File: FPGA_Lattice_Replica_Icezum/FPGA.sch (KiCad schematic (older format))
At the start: 33 parts, among them U1 iCE40HX1K-TQ144, U2 N25Q032A

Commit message: se finalizo asignación de footprint de acuerdo al modelo original de la icezum alhambra
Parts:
- C12, C13, C14, C15, C16: footprint (none) -> footprints:C_0402
- FID1, FID2, FID3: footprint (none) -> footprints:Fiducial
- LD10: footprint (none) -> footprints:LED_0603
- R1, R2, R3, R4, R46, R5, R6, R7, R8, R9: footprint (none) -> footprints:R_0402
- U1: footprint (none) -> footprints:TQFP-144_IPC-MD
- U2: footprint (none) -> footprints:DFN-8-6x5mm
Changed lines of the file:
@@
 F 0 "U1" H 1950 1587 60  0000 C CNN
 F 1 "iCE40HX1K-TQ144" H 1950 1481 60  0000 C CNN
-F 2 "" H 1600 100 60  0001 C CNN
+F 2 "footprints:TQFP-144_IPC-MD" H 1600 100 60  0001 C CNN
 F 3 "" H 1600 100 60  0000 C CNN
 	1    1250 1300
@@
 F 0 "U1" H 2550 4887 60  0000 C CNN
 F 1 "iCE40HX1K-TQ144" H 2550 4781 60  0000 C CNN
-F 2 "" H 2200 3400 60  0001 C CNN
+F 2 "footprints:TQFP-144_IPC-MD" H 2200 3400 60  0001 C CNN
 F 3 "" H 2200 3400 60  0000 C CNN
 	2    1850 4600
@@
 F 0 "U1" H 6150 1617 60  0000 C CNN
 F 1 "iCE40HX1K-TQ144" H 6150 1511 60  0000 C CNN
-F 2 "" H 5800 150 60  0001 C CNN
+F 2 "footprints:TQFP-144_IPC-MD" H 5800 150 60  0001 C CNN
 F 3 "" H 5800 150 60  0000 C CNN
 	3    5450 1350
@@
 F 0 "U1" H 9400 1617 60  0000 C CNN
 F 1 "iCE40HX1K-TQ144" H 9400 1511 60  0000 C CNN
-F 2 "" H 9050 150 60  0001 C CNN
+F 2 "footprints:TQFP-144_IPC-MD" H 9050 150 60  0001 C CNN
 F 3 "" H 9050 150 60  0000 C CNN
 	4    8700 1350
@@
 F 0 "U1" H 5600 5467 60  0000 C CNN
 F 1 "iCE40HX1K-TQ144" H 5600 5361 60  0000 C CNN
-F 2 "" H 5250 4000 60  0001 C CNN
+F 2 "footprints:TQFP-144_IPC-MD" H 5250 4000 60  0001 C CNN
 F 3 "" H 5250 4000 60  0000 C CNN
 	5    4900 5200
@@
 F 0 "U1" H 9850 4717 60  0000 C CNN
 F 1 "iCE40HX1K-TQ144" H 9850 4611 60  0000 C CNN
-F 2 "" H 9500 3250 60  0001 C CNN
+F 2 "footprints:TQFP-144_IPC-MD" H 9500 3250 60  0001 C CNN
 F 3 "" H 9500 3250 60  0000 C CNN
 	6    9150 4450
@@
 F 0 "R2" V 4750 2700 50  0000 C CNN
 F 1 "10K±5% 0.063W" V 4900 2550 50  0000 C CNN
-F 2 "" V 4730 2550 50  0001 C CNN
+F 2 "footprints:R_0402" V 4730 2550 50  0001 C CNN
 F 3 "~" H 4800 2550 50  0001 C CNN
 	1    4800 2550
@@
 F 0 "R3" V 4650 3000 50  0000 C CNN
 F 1 "10K±5% 0.063W" V 4850 3000 50  0000 C CNN
-F 2 "" V 4680 3000 50  0001 C CNN
+F 2 "footprints:R_0402" V 4680 3000 50  0001 C CNN
 F 3 "~" H 4750 3000 50  0001 C CNN
 	1    4750 3000
@@
 F 0 "R1" V 4693 2200 50  0000 C CNN
 F 1 "10K±5% 0.063W" V 4784 2200 50  0000 C CNN
-F 2 "" V 4830 2200 50  0001 C CNN
+F 2 "footprints:R_0402" V 4830 2200 50  0001 C CNN
 F 3 "~" H 4900 2200 50  0001 C CNN
 	1    4900 2200
@@
 F 0 "U2" H 7350 5400 60  0000 C CNN
 F 1 "N25Q032A" H 7400 4800 60  0000 C CNN
-F 2 "" H 7180 5300 60  0001 C CNN
+F 2 "footprints:DFN-8-6x5mm" H 7180 5300 60  0001 C CNN
 F 3 "" H 7180 5300 60  0000 C CNN
 	1    6650 5200
@@
 F 0 "LD10" H 5143 6745 50  0000 C CNN
 F 1 "Yellow" H 5143 6836 50  0000 C CNN
-F 2 "" H 5150 7000 50  0001 C CNN
+F 2 "footprints:LED_0603" H 5150 7000 50  0001 C CNN
 F 3 "~" H 5150 7000 50  0001 C CNN
 	1    5150 7000
@@
 F 0 "R6" H 7700 4750 50  0000 L CNN
 F 1 "10K±5% 0.063W" V 7600 4250 50  0000 L CNN
-F 2 "" V 7630 4600 50  0001 C CNN
+F 2 "footprints:R_0402" V 7630 4600 50  0001 C CNN
 F 3 "~" H 7700 4600 50  0001 C CNN
 	1    7700 4600
@@
 F 0 "R7" H 7950 4750 50  0000 L CNN
 F 1 "10K±5% 0.063W" V 7850 4250 50  0000 L CNN
-F 2 "" V 7880 4600 50  0001 C CNN
+F 2 "footprints:R_0402" V 7880 4600 50  0001 C CNN
 F 3 "~" H 7950 4600 50  0001 C CNN
 	1    7950 4600
@@
 F 0 "R8" H 8200 4750 50  0000 L CNN
 F 1 "10K±5% 0.063W" V 8100 4250 50  0000 L CNN
-F 2 "" V 8130 4600 50  0001 C CNN
+F 2 "footprints:R_0402" V 8130 4600 50  0001 C CNN
 F 3 "~" H 8200 4600 50  0001 C CNN
 	1    8200 4600
@@
 F 0 "R46" V 5543 7000 50  0000 C CNN
 F 1 "2K2±5% 0.063W" V 5634 7000 50  0000 C CNN
-F 2 "" V 5680 7000 50  0001 C CNN
+F 2 "footprints:R_0402" V 5680 7000 50  0001 C CNN
 F 3 "~" H 5750 7000 50  0001 C CNN
 	1    5750 7000
@@
 F 0 "R5" H 6520 4496 50  0000 L CNN
 F 1 "10K±5% 0.063W" V 6350 4150 50  0000 L CNN
-F 2 "" V 6380 4450 50  0001 C CNN
+F 2 "footprints:R_0402" V 6380 4450 50  0001 C CNN
 F 3 "~" H 6450 4450 50  0001 C CNN
 	1    6450 4450
@@
 F 0 "R4" V 1293 6000 50  0000 C CNN
 F 1 "10K±5% 0.063W" V 1384 6000 50  0000 C CNN
-F 2 "" V 1430 6000 50  0001 C CNN
+F 2 "footprints:R_0402" V 1430 6000 50  0001 C CNN
 F 3 "~" H 1500 6000 50  0001 C CNN
 	1    1500 6000
@@
 F 0 "C12" H 9000 5550 50  0000 L CNN
 F 1 "100 nF" H 9015 5455 50  0000 L CNN
-F 2 "" H 8938 5350 50  0001 C CNN
+F 2 "footprints:C_0402" H 8938 5350 50  0001 C CNN
 F 3 "~" H 8900 5500 50  0001 C CNN
 	1    8900 5500
@@
 F 0 "R9" H 8520 5146 50  0000 L CNN
 F 1 "100K±5% 0.063W" V 8350 4800 50  0000 L CNN
-F 2 "" V 8380 5100 50  0001 C CNN
+F 2 "footprints:R_0402" V 8380 5100 50  0001 C CNN
 F 3 "~" H 8450 5100 50  0001 C CNN
 	1    8450 5100
@@
 F 0 "C16" H 10815 6096 50  0000 L CNN
 F 1 "100 nF" H 10750 5950 50  0000 L CNN
-F 2 "" H 10738 5900 50  0001 C CNN
+F 2 "footprints:C_0402" H 10738 5900 50  0001 C CNN
 F 3 "~" H 10700 6050 50  0001 C CNN
 	1    10700 6050
@@
 F 0 "C15" H 10415 6096 50  0000 L CNN
 F 1 "100 nF" H 10350 5950 50  0000 L CNN
-F 2 "" H 10338 5900 50  0001 C CNN
+F 2 "footprints:C_0402" H 10338 5900 50  0001 C CNN
 F 3 "~" H 10300 6050 50  0001 C CNN
 	1    10300 6050
@@
 F 0 "C14" H 10015 6096 50  0000 L CNN
 F 1 "100 nF" H 9950 5950 50  0000 L CNN
-F 2 "" H 9938 5900 50  0001 C CNN
+F 2 "footprints:C_0402" H 9938 5900 50  0001 C CNN
 F 3 "~" H 9900 6050 50  0001 C CNN
 	1    9900 6050
@@
 F 0 "C13" H 9650 6100 50  0000 L CNN
 F 1 "100 nF" H 9550 5950 50  0000 L CNN
-F 2 "" H 9588 5900 50  0001 C CNN
+F 2 "footprints:C_0402" H 9588 5900 50  0001 C CNN
 F 3 "~" H 9550 6050 50  0001 C CNN
 	1    9550 6050
@@
 F 0 "FID1" H 1678 7303 59  0000 L CNN
 F 1 "FIDUCIAL" H 1678 7198 59  0000 L CNN
-F 2 "" H 1450 7250 157 0001 C CNN
+F 2 "footprints:Fiducial" H 1450 7250 157 0001 C CNN
 F 3 "" H 1450 7250 157 0000 C CNN
 	1    1450 7250
@@
 F 0 "FID2" H 2728 7303 59  0000 L CNN
 F 1 "FIDUCIAL" H 2728 7198 59  0000 L CNN
-F 2 "" H 2500 7250 157 0001 C CNN
+F 2 "footprints:Fiducial" H 2500 7250 157 0001 C CNN
 F 3 "" H 2500 7250 157 0000 C CNN
 	1    2500 7250
@@
 F 0 "FID3" H 3678 7303 59  0000 L CNN
 F 1 "FIDUCIAL" H 3678 7198 59  0000 L CNN
-F 2 "" H 3450 7250 157 0001 C CNN
+F 2 "footprints:Fiducial" H 3450 7250 157 0001 C CNN
 F 3 "" H 3450 7250 157 0000 C CNN
 	1    3450 7250

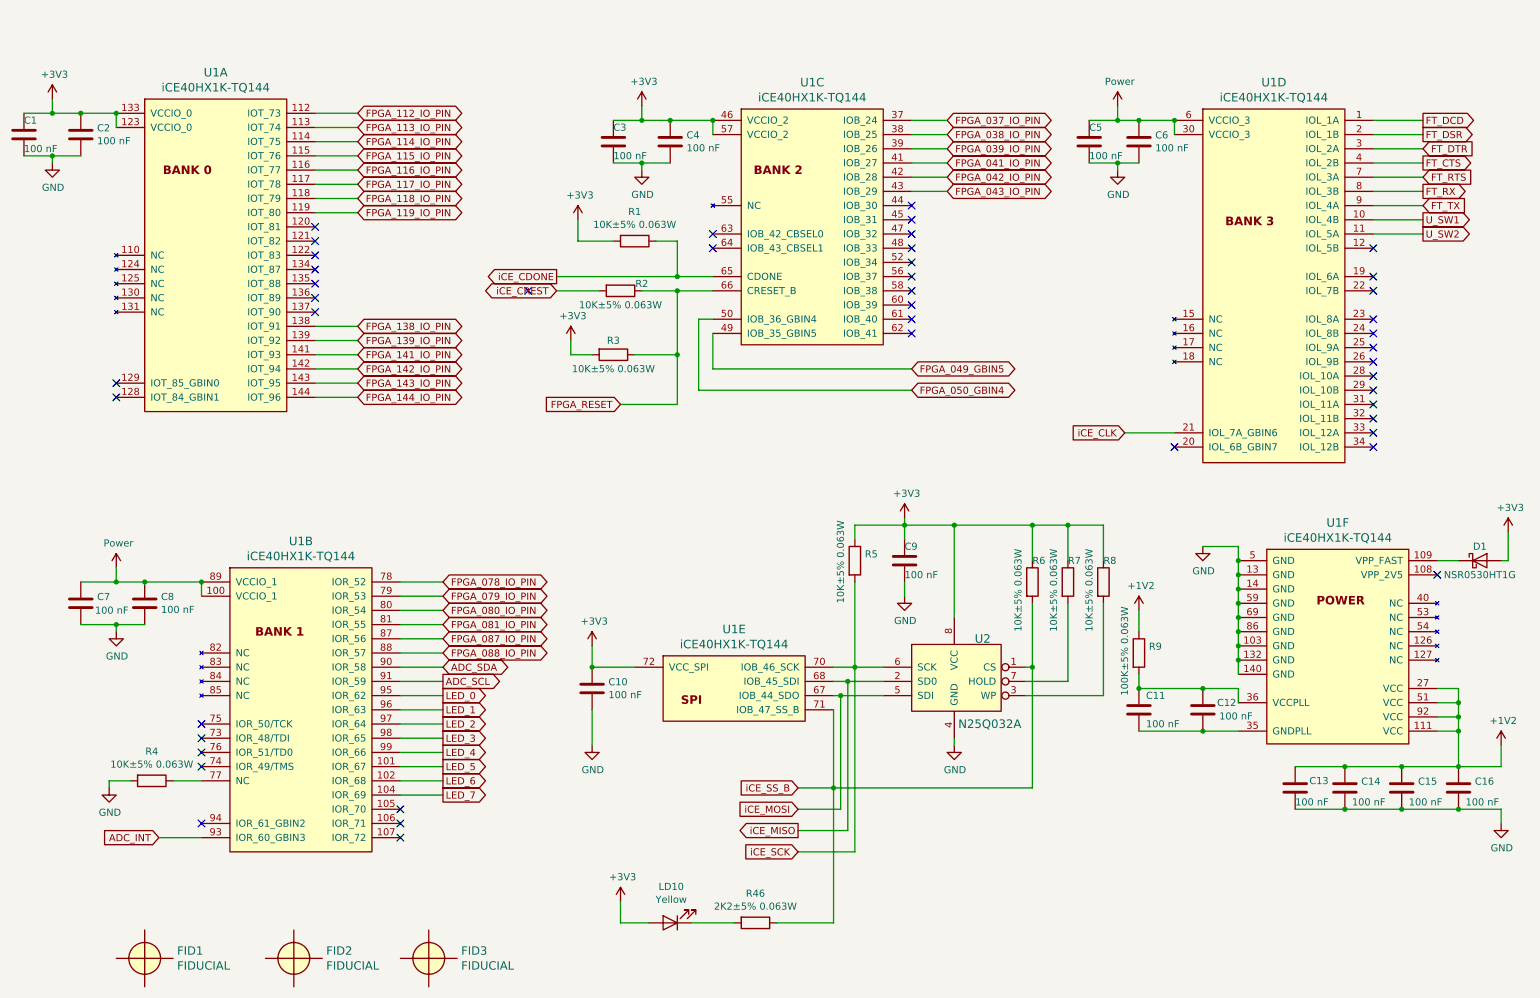
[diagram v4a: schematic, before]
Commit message: se coloco hojas de datos de los componentes
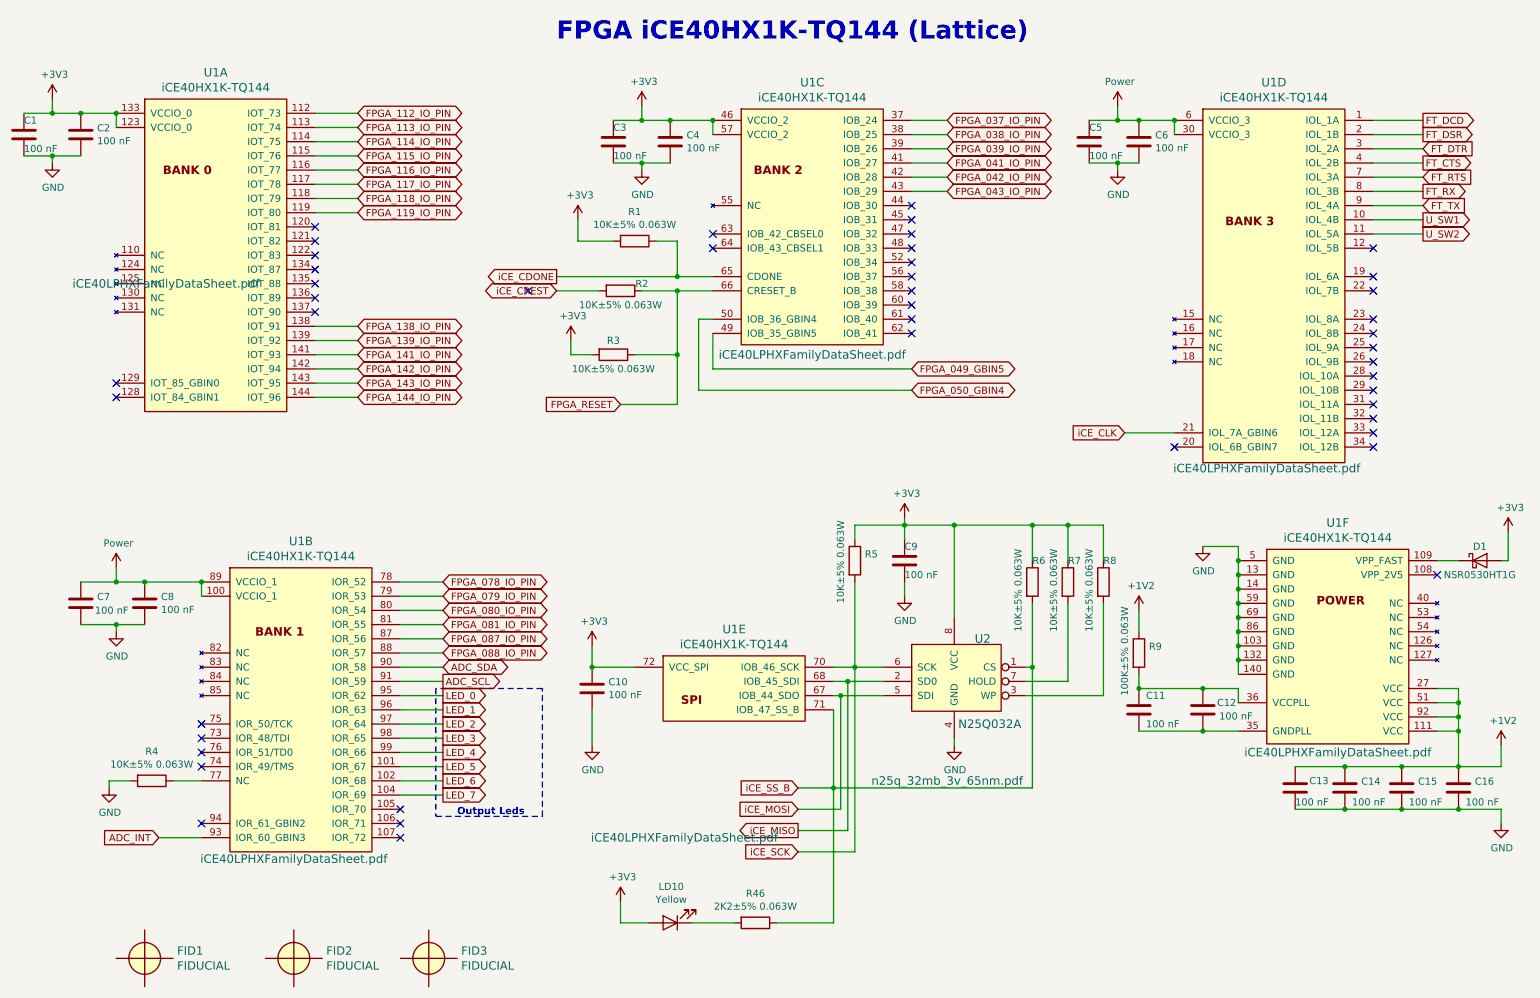
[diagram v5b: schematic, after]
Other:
- note added: "FPGA iCE40HX1K-TQ144 (Lattice)"
- note added: "Output Leds"
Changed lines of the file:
@@
 F 1 "iCE40HX1K-TQ144" H 1950 1481 60  0000 C CNN
 F 2 "footprints:TQFP-144_IPC-MD" H 1600 100 60  0001 C CNN
-F 3 "" H 1600 100 60  0000 C CNN
+F 3 "iCE40LPHXFamilyDataSheet.pdf" H 1600 100 60  0000 C CNN
 	1    1250 1300
 	1    0    0    -1
@@
 F 1 "iCE40HX1K-TQ144" H 2550 4781 60  0000 C CNN
 F 2 "footprints:TQFP-144_IPC-MD" H 2200 3400 60  0001 C CNN
-F 3 "" H 2200 3400 60  0000 C CNN
+F 3 "iCE40LPHXFamilyDataSheet.pdf" H 2500 2650 60  0000 C CNN
 	2    1850 4600
 	1    0    0    -1
@@
 F 1 "iCE40HX1K-TQ144" H 6150 1511 60  0000 C CNN
 F 2 "footprints:TQFP-144_IPC-MD" H 5800 150 60  0001 C CNN
-F 3 "" H 5800 150 60  0000 C CNN
+F 3 "iCE40LPHXFamilyDataSheet.pdf" H 6150 -300 60  0000 C CNN
 	3    5450 1350
 	1    0    0    -1
@@
 F 1 "iCE40HX1K-TQ144" H 9400 1511 60  0000 C CNN
 F 2 "footprints:TQFP-144_IPC-MD" H 9050 150 60  0001 C CNN
-F 3 "" H 9050 150 60  0000 C CNN
+F 3 "iCE40LPHXFamilyDataSheet.pdf" H 9350 -1100 60  0000 C CNN
 	4    8700 1350
 	1    0    0    -1
@@
 F 1 "iCE40HX1K-TQ144" H 5600 5361 60  0000 C CNN
 F 2 "footprints:TQFP-144_IPC-MD" H 5250 4000 60  0001 C CNN
-F 3 "" H 5250 4000 60  0000 C CNN
+F 3 "iCE40LPHXFamilyDataSheet.pdf" H 5250 4000 60  0000 C CNN
 	5    4900 5200
 	1    0    0    -1
@@
 F 1 "iCE40HX1K-TQ144" H 9850 4611 60  0000 C CNN
 F 2 "footprints:TQFP-144_IPC-MD" H 9500 3250 60  0001 C CNN
-F 3 "" H 9500 3250 60  0000 C CNN
+F 3 "iCE40LPHXFamilyDataSheet.pdf" H 9850 3100 60  0000 C CNN
 	6    9150 4450
 	1    0    0    -1
@@
 F 1 "N25Q032A" H 7400 4800 60  0000 C CNN
 F 2 "footprints:DFN-8-6x5mm" H 7180 5300 60  0001 C CNN
-F 3 "" H 7180 5300 60  0000 C CNN
+F 3 "n25q_32mb_3v_65nm.pdf" H 7100 4400 60  0000 C CNN
 	1    6650 5200
 	1    0    0    -1
@@
 NoConn ~ 10550 4550
 NoConn ~ 1850 6300
+Text Notes 4350 800  0    129  ~ 26
+FPGA iCE40HX1K-TQ144 (Lattice)
+Wire Notes Line
+	4250 5350 3500 5350
+Wire Notes Line
+	3500 5350 3500 6250
+Wire Notes Line
+	3500 6250 4250 6250
+Wire Notes Line
+	4250 6250 4250 5350
+Text Notes 3650 6250 0    50   ~ 10
+Output Leds
 $EndSCHEMATC

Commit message: se realizo las correcciones sugeridas por el revisor
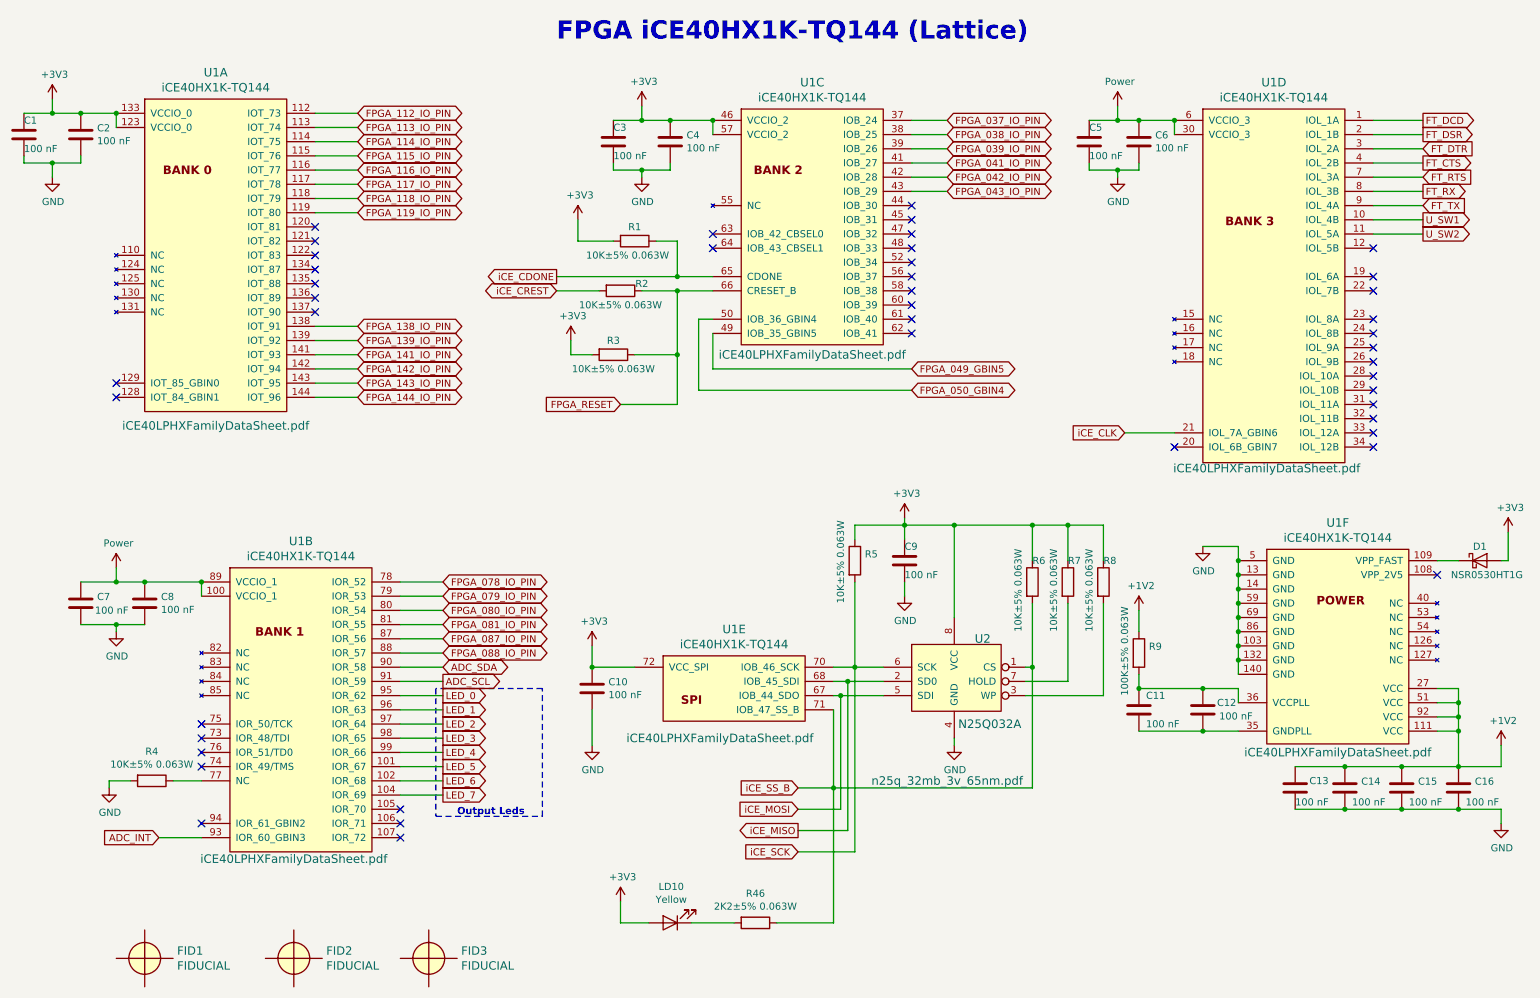
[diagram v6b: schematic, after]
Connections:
- no-connect marks 45 -> 44
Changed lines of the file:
@@
 F 1 "iCE40HX1K-TQ144" H 1950 1481 60  0000 C CNN
 F 2 "footprints:TQFP-144_IPC-MD" H 1600 100 60  0001 C CNN
-F 3 "iCE40LPHXFamilyDataSheet.pdf" H 1600 100 60  0000 C CNN
+F 3 "iCE40LPHXFamilyDataSheet.pdf" H 1950 -900 60  0000 C CNN
 	1    1250 1300
 	1    0    0    -1
@@
 $Comp
 L icezum:iCE40HX1K-TQ144 U1
-U 4 1 5CF9D9CD
-P 8700 1350
-F 0 "U1" H 9400 1617 60  0000 C CNN
-F 1 "iCE40HX1K-TQ144" H 9400 1511 60  0000 C CNN
-F 2 "footprints:TQFP-144_IPC-MD" H 9050 150 60  0001 C CNN
-F 3 "iCE40LPHXFamilyDataSheet.pdf" H 9350 -1100 60  0000 C CNN
-	4    8700 1350
-	1    0    0    -1
-$EndComp
-$Comp
-L icezum:iCE40HX1K-TQ144 U1
 U 5 1 5CFA1DD3
 P 4900 5200
@@
 F 1 "iCE40HX1K-TQ144" H 5600 5361 60  0000 C CNN
 F 2 "footprints:TQFP-144_IPC-MD" H 5250 4000 60  0001 C CNN
-F 3 "iCE40LPHXFamilyDataSheet.pdf" H 5250 4000 60  0000 C CNN
+F 3 "iCE40LPHXFamilyDataSheet.pdf" H 5500 4700 60  0000 C CNN
 	5    4900 5200
 	1    0    0    -1
@@
 	1000 1300 800  1300
 Wire Wire Line
-	600  1600 800  1600
-Wire Wire Line
 	5150 1350 4950 1350
-Wire Wire Line
-	4750 1650 4950 1650
 Text GLabel 2950 1300 2    50   BiDi ~ 0
 FPGA_112_IO_PIN
@@
 U 1 1 5CFDDF44
 P 4900 2200
-F 0 "R1" V 4693 2200 50  0000 C CNN
-F 1 "10K±5% 0.063W" V 4784 2200 50  0000 C CNN
+F 0 "R1" V 4800 2200 50  0000 C CNN
+F 1 "10K±5% 0.063W" V 5000 2150 50  0000 C CNN
 F 2 "footprints:R_0402" V 4830 2200 50  0001 C CNN
 F 3 "~" H 4900 2200 50  0001 C CNN
@@
 L power:GND #PWR0133
 U 1 1 5D03AF49
-P 800 1650
-F 0 "#PWR0133" H 800 1400 50  0001 C CNN
-F 1 "GND" H 805 1477 50  0000 C CNN
-F 2 "" H 800 1650 50  0001 C CNN
-F 3 "" H 800 1650 50  0001 C CNN
-	1    800  1650
+P 800 1750
+F 0 "#PWR0133" H 800 1500 50  0001 C CNN
+F 1 "GND" H 805 1577 50  0000 C CNN
+F 2 "" H 800 1750 50  0001 C CNN
+F 3 "" H 800 1750 50  0001 C CNN
+	1    800  1750
 	1    0    0    -1
 $EndComp
@@
 NoConn ~ 2650 2500
 NoConn ~ 2650 2600
-Wire Wire Line
-	800  1650 800  1600
-Connection ~ 800  1600
-Wire Wire Line
-	800  1600 1000 1600
 Wire Wire Line
 	800  1200 800  1300
@@
 L power:GND #PWR0136
 U 1 1 5D0DDC54
-P 4950 1700
-F 0 "#PWR0136" H 4950 1450 50  0001 C CNN
-F 1 "GND" H 4955 1527 50  0000 C CNN
-F 2 "" H 4950 1700 50  0001 C CNN
-F 3 "" H 4950 1700 50  0001 C CNN
-	1    4950 1700
+P 4950 1750
+F 0 "#PWR0136" H 4950 1500 50  0001 C CNN
+F 1 "GND" H 4955 1577 50  0000 C CNN
+F 2 "" H 4950 1750 50  0001 C CNN
+F 3 "" H 4950 1750 50  0001 C CNN
+	1    4950 1750
 	1    0    0    -1
 $EndComp
@@
 Connection ~ 5150 1350
 Connection ~ 5450 1350
-Wire Wire Line
-	4950 1700 4950 1650
-Connection ~ 4950 1650
-Wire Wire Line
-	4950 1650 5150 1650
 NoConn ~ 5450 2150
 NoConn ~ 5450 2250
@@
 L power:GND #PWR0139
 U 1 1 5D193C6D
-P 8300 1700
-F 0 "#PWR0139" H 8300 1450 50  0001 C CNN
-F 1 "GND" H 8305 1527 50  0000 C CNN
-F 2 "" H 8300 1700 50  0001 C CNN
-F 3 "" H 8300 1700 50  0001 C CNN
-	1    8300 1700
-	1    0    0    -1
-$EndComp
-Wire Wire Line
-	8100 1650 8300 1650
-Wire Wire Line
-	8300 1650 8300 1700
-Wire Wire Line
-	8300 1650 8450 1650
-Connection ~ 8300 1650
+P 8300 1750
+F 0 "#PWR0139" H 8300 1500 50  0001 C CNN
+F 1 "GND" H 8305 1577 50  0000 C CNN
+F 2 "" H 8300 1750 50  0001 C CNN
+F 3 "" H 8300 1750 50  0001 C CNN
+	1    8300 1750
+	1    0    0    -1
+$EndComp
 Wire Wire Line
 	8100 1350 8300 1350
@@
 Wire Wire Line
 	8700 1450 8700 1350
-Connection ~ 8700 1350
 $Comp
 L power:GND #PWR0140
@@
 P 10850 4450
 F 0 "D1" H 10850 4550 50  0000 C CNN
-F 1 "NSR0530HT1G" H 10850 4350 50  0000 C CNN
+F 1 "NSR0530HT1G" H 10900 4350 50  0000 C CNN
 F 2 "footprints:SOD-323" H 10850 4450 50  0001 C CNN
 F 3 "~" H 10850 4450 50  0001 C CNN
@@
 $EndComp
 NoConn ~ 2650 2700
-NoConn ~ 4150 2550
 NoConn ~ 10550 4550
 NoConn ~ 1850 6300
@@
 Text Notes 3650 6250 0    50   ~ 10
 Output Leds
+Wire Wire Line
+	600  1600 600  1650
+Wire Wire Line
+	600  1650 800  1650
+Wire Wire Line
+	800  1650 800  1750
+Wire Wire Line
+	800  1650 1000 1650
+Wire Wire Line
+	1000 1650 1000 1600
+Connection ~ 800  1650
+Wire Wire Line
+	4750 1650 4750 1700
+Wire Wire Line
+	4750 1700 4950 1700
+Wire Wire Line
+	4950 1700 4950 1750
+Wire Wire Line
+	4950 1700 5150 1700
+Wire Wire Line
+	5150 1700 5150 1650
+Connection ~ 4950 1700
+Wire Wire Line
+	8100 1650 8100 1700
+Wire Wire Line
+	8100 1700 8300 1700
+Wire Wire Line
+	8300 1700 8300 1750
+Wire Wire Line
+	8300 1700 8450 1700
+Wire Wire Line
+	8450 1700 8450 1650
+Connection ~ 8300 1700
+Connection ~ 8700 1350
+$Comp
+L icezum:iCE40HX1K-TQ144 U1
+U 4 1 5CF9D9CD
+P 8700 1350
+F 0 "U1" H 9400 1617 60  0000 C CNN
+F 1 "iCE40HX1K-TQ144" H 9400 1511 60  0000 C CNN
+F 2 "footprints:TQFP-144_IPC-MD" H 9050 150 60  0001 C CNN
+F 3 "iCE40LPHXFamilyDataSheet.pdf" H 9350 -1100 60  0000 C CNN
+	4    8700 1350
+	1    0    0    -1
+$EndComp
 $EndSCHEMATC
